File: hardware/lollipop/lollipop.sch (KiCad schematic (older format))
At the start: 88 parts

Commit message: loop filter
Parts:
- added C? (x2): 100pF, symbol C
- added C? (x2): 330pF, symbol C
- added C?: 82pF, symbol C
- added C?: 180pF, symbol C
- added R? (x2): 470, symbol R
- added R?: 22k, symbol R
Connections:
- net GND: now also C?.2, C?.2, C?.2, C?.2
- net VCC: now also C?.1, C?.1
- net GPO5: now reaches U?.1 (ENBL/GPO5)
- net GPO1: now reaches U?.15 (GPO1/ADD1)
- net GPO2: now reaches U?.16 (GPO2/ADD2)
- net GPO3: now reaches U?.25 (GPO3/FM)
- net GPO4: now reaches U?.26 (GPO4/LD/DO)
- net ENX: now reaches U?.30 (ENX)
- net SCLK: now reaches U?.31 (SCLK)
- net SDATA: now reaches U?.32 (SDATA)
- net at U?.6 (LFILT1): now also C?.2, R?.1
- net at U?.7 (LFITLT2): now also C?.1, C?.1, R?.1
- net at U?.8 (LFILT3): now also C?.1, R?.2
- net GPO6: now reaches U?.9 (MODE/GPO6)
- new net: C?.1, R?.1, R?.2
- new net: C?.2, R?.2
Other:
- note added: "loop filter"
- note added: "serial"

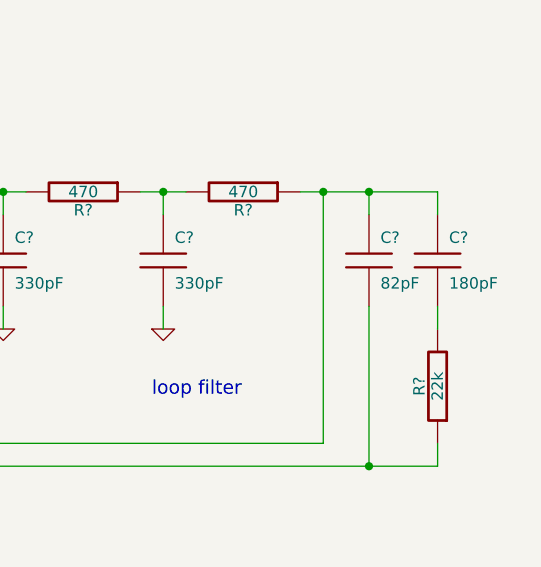
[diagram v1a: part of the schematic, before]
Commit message: loop filter correction
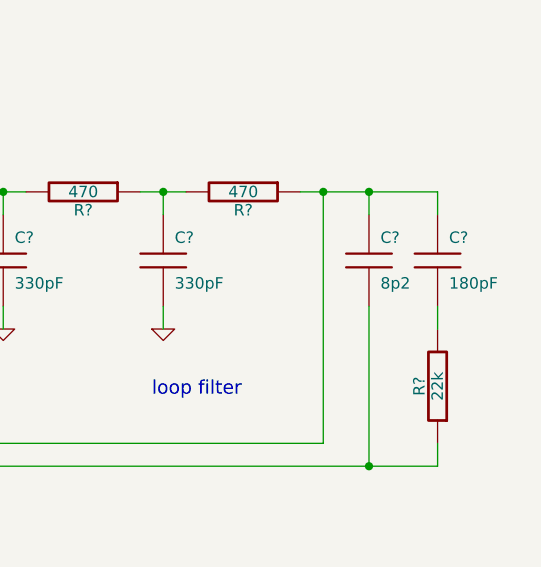
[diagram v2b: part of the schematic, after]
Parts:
- C?: value 82pF -> 8p2
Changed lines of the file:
@@
-EESchema Schematic File Version 2  date Sat May 12 14:39:51 2012
+EESchema Schematic File Version 2  date Sat May 12 14:43:51 2012
 LIBS:power
 LIBS:device
@@
 P 15600 4100
 F 0 "C?" H 15650 4200 50  0000 L CNN
-F 1 "82pF" H 15650 4000 50  0000 L CNN
+F 1 "8p2" H 15650 4000 50  0000 L CNN
 	1    15600 4100
 	1    0    0    -1

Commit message: spi header, misc. mixer stuff
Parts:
- added C? (x7): 33pF, symbol C
- added C? (x3): 10nF, symbol C
- added C?: 1nF, symbol C
- added P?: SPI, symbol CONN_5
- added R?: 51k, symbol R
- added R? (x2): R, symbol R
- L? (x4): value INDUCTOR -> 47nH
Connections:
- net ENX: now also C?.1, P?.3, R?.2
- net GND: now also U?.12 (TM), C?.2, C?.2, C?.2, C?.2, C?.2, C?.2, C?.2, C?.2, C?.2, C?.2, P?.1, R?.1
- net SCLK: now also C?.1, P?.4
- net SDATA: now also C?.1, P?.5
- net VCC: now also U?.5 (ANA_VDD1), C?.1, C?.1, C?.1, C?.1, C?.1, C?.1, R?.1, R?.1
- net at U?.10 (REF_IN): now also C?.2
- net RESETX: now reaches U?.29 (RESETX)
- net RESETX: now also C?.1, P?.2, R?.2
- net at U?.4 (REXT): now also R?.2
- new net CLK: C?.1
- no-connect marks 0 -> 2
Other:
- note added: "1%"
- note added: "TO DO:\ncheck balun pinouts\nswitch control logic\npower in header\nclock in header\nimpedance matching\namplification\nconfirm mixer output inductor values"
- note removed: "TO DO:\nmixer output inductor values\ncheck balun pinouts\nswitch control logic\ncontrol header\npower in header\nclock in header\nimpedance matching\namplification\nmisc. mixer connections"
- note removed: "serial"

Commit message: switch control logic
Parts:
- added C? (x2): C, symbol C
- added U?: GSG-74HC08, symbol GSG-74HC08
- added U?: GSG-74HC04, symbol GSG-74HC04
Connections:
- net GPO1 is gone; now on net SWTXB1: U?.15 (GPO1/ADD1)
- net GPO2 is gone; now on net SWRXB1: U?.16 (GPO2/ADD2)
- net GPO3 is gone; now on net SWTXA1: U?.25 (GPO3/FM)
- net GPO4 is gone; now on net SWRXA1: U?.26 (GPO4/LD/DO)
- net GPO5 is gone; now on net SWD1: U?.1 (ENBL/GPO5)
- net SWRXV1 is gone; now on net SWRXB2: U?.3 (V1)
- net SWTXV3 is gone; now on net SWTXB1: U?.7 (V3)
- net GND: now also C?.2, C?.2, U?.7 (GND), U?.7 (GND)
- net SWD1: now also U?.11 (5A)
- net SWD2: now also U?.10 (5Y)
- net SWRXA1: now also U?.5 (2B), U?.9 (4A)
- net SWRXA2: now also U?.2 (1B), U?.8 (4Y)
- net SWRXB1: now also U?.1 (1A), U?.3 (2A), U?.4 (2A)
- net SWRXB2: now also U?.4 (2Y)
- net SWRXV2: now also U?.3 (1Y)
- net SWRXV3: now also U?.6 (2Y)
- net SWTXA1: now also U?.12 (4A), U?.5 (3A)
- net SWTXA2: now also U?.6 (3Y), U?.9 (3A)
- net SWTXB1: now also U?.1 (1A)
- net SWTXB2: now also U?.10 (3B), U?.13 (4B), U?.2 (1Y)
- net SWTXV1: now also U?.8 (3Y)
- net SWTXV2: now also U?.11 (4Y)
- net VCC: now also C?.1, C?.1, U?.14 (VCC), U?.14 (VCC)
- no-connect marks 2 -> 4
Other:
- note added: "TO DO:\ncheck balun pinouts\npower in header\nclock in header\nimpedance matching\namplification\nconfirm mixer output inductor values\nTVS\namp control logic?"
- note added: "switch control logic ensures valid switch configurations"
- note removed: "TO DO:\ncheck balun pinouts\nswitch control logic\npower in header\nclock in header\nimpedance matching\namplification\nconfirm mixer output inductor values"

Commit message: switch control header
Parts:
- added P?: CONN_7X2, symbol CONN_7X2
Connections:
- net GND: now also P?.13, P?.14
- net GPO6: now also P?.12
- net SWD1: now also P?.9; no longer U?.1 (ENBL/GPO5)
- net SWRXA1: now also P?.7 (P7); no longer U?.26 (GPO4/LD/DO)
- net SWRXB1: now also P?.3 (P3); no longer U?.16 (GPO2/ADD2)
- net SWTXA1: now also P?.5 (P5); no longer U?.25 (GPO3/FM)
- net SWTXB1: now also P?.1 (P1); no longer U?.15 (GPO1/ADD1)
- new net GPO1: P?.2 (P2), U?.15 (GPO1/ADD1)
- new net GPO2: P?.4 (P4), U?.16 (GPO2/ADD2)
- new net GPO3: P?.6 (P6), U?.25 (GPO3/FM)
- new net GPO4: P?.8 (P8), U?.26 (GPO4/LD/DO)
- new net GPO5: P?.10, U?.1 (ENBL/GPO5)
- no-connect marks 4 -> 5
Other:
- note added: "install jumpers for switch\ncontrol via the RFFC5071"

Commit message: TVS diodes
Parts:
- added C?: DNP, symbol C
- added D? (x2): GSG-DIODE-TVS-BI, symbol GSG-DIODE-TVS-BI
- added P?: VCC, symbol CONN_3X2
- added P?: CLK, symbol CONN_2
- P?: value GSG-SMA-CONN -> RX-only
- P?: value GSG-SMA-CONN -> TX/RX
- P?: value CONN_7X2 -> SWITCH_CTRL
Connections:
- net CLK: now also P?.2 (PM)
- net GND: now also C?.2, D?.1 (A), D?.1 (A), P?.1, P?.1 (P1), P?.3, P?.5
- net VCC: now also P?.2, P?.4, P?.6
- net at C?.2, P?.1 (RF): now also D?.2 (K) (x2)
- net REF_IN: now reaches C?.2, U?.10 (REF_IN)
- net REF_IN: now also C?.1
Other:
- note added: "TO DO:\ncheck balun pinouts\nimpedance matching\namplification\nconfirm mixer output inductor values\namp control logic?"
- note removed: "RX only"
- note removed: "TO DO:\ncheck balun pinouts\npower in header\nclock in header\nimpedance matching\namplification\nconfirm mixer output inductor values\nTVS\namp control logic?"
- note removed: "TX/RX"
- moved on the sheet: C?, P?

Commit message: fixed balun pinouts
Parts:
- removed D?: GSG-DIODE-TVS-BI, symbol GSG-DIODE-TVS-BI
- removed T? (x2): BALUN, symbol BALUN
- added D?: GSG-DIODE-TVS-BI, symbol GSG-DIODE-TVS-BI
- added T? (x2): BALUN-CX2156NL, symbol BALUN-CX2156NL
- D?: Description (none) -> CERAMIC ESD DEV .5PF 7V SMD; Manufacturer (none) -> Murata; Part Number (none) -> LXES1UBBB1-008
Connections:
- net GND: now also T?.2 (S2), T?.2 (S2), D?.1 (A), T?.1 (PR2), T?.1 (PR2); no longer T?.1 (S1), T?.1 (S1)
- net at U?.1 (IN): now also T?.3 (PR1) (x2)
- net at C?.2: now also T?.6 (S2) (x2)
- net at C?.2: now also T?.4 (S1) (x2)
- net at C?.2, P?.1 (RF): now also D?.2 (K)
- net at P?.1 (RF): now also T?.1 (S1); no longer T?.2 (S2) (x2)
- net at T?.3 (PR1): now also C?.2; no longer C?.2
- net at T?.4 (PR2): now also C?.2; no longer C?.2
- net at C?.2: now also T?.3 (PR1); no longer T?.4 (PR2)
- net at C?.2: now also T?.4 (PR2); no longer T?.3 (PR1)

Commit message: added exposed paddle to mixer symbol
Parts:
- R? (x2): value R -> 4k7
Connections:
- net GND: now also U?.0 (EP)
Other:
- note added: "TO DO:\nimpedance matching\namplification\nconfirm mixer output inductor values\namp control logic?"
- note removed: "TO DO:\ncheck balun pinouts\nimpedance matching\namplification\nconfirm mixer output inductor values\namp control logic?"
